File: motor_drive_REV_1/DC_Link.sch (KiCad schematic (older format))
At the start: 5 parts

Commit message: organizing pinout and BOM
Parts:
- removed M? (x2): Conn_01x01, symbol Connector_Generic:Conn_01x01
- removed R? (x2): R_Shunt, symbol motor_drive:R_Shunt
- added C13: 0.01uF, motor_drive_footprints:C_0603_1608Metric, symbol motor_drive:C
- added R19, R20: R, motor_drive_footprints:C_0603_1608Metric, symbol motor_drive:R
- R18: renamed from R?; footprint (none) -> motor_drive_footprints:C_0603_1608Metric
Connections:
- net labels added: 5.0V, DC_neg_in, DC_pos_in, GND
- net labels removed: DC+, DC-
- wire segments 12 -> 14
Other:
- moved on the sheet: R18
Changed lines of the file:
@@
 $Descr A4 11693 8268
 encoding utf-8
-Sheet 12 14
+Sheet 9 14
 Title ""
 Date ""
@@
 $EndDescr
 $Comp
-L Connector_Generic:Conn_01x01 M?
-U 1 1 5E3365D3
-P 4900 4150
-AR Path="/5E3365D3" Ref="M?"  Part="1"
-AR Path="/5E257703/5E3365D3" Ref="M?"  Part="1"
-F 0 "M?" H 4980 4146 50  0000 L CNN
-F 1 "Conn_01x01" H 4980 4101 50  0001 L CNN
-F 2 "" H 4900 4150 50  0001 C CNN
-F 3 "~" H 4900 4150 50  0001 C CNN
-	1    4900 4150
-	-1   0    0    1
-$EndComp
-$Comp
-L Connector_Generic:Conn_01x01 M?
-U 1 1 5E3365D9
-P 4900 2900
-AR Path="/5E3365D9" Ref="M?"  Part="1"
-AR Path="/5E257703/5E3365D9" Ref="M?"  Part="1"
-F 0 "M?" H 4980 2896 50  0000 L CNN
-F 1 "Conn_01x01" H 4980 2851 50  0001 L CNN
-F 2 "" H 4900 2900 50  0001 C CNN
-F 3 "~" H 4900 2900 50  0001 C CNN
-	1    4900 2900
-	-1   0    0    1
-$EndComp
-Text GLabel 6500 2900 2    50   Input ~ 0
-DC+
-Text GLabel 6550 4150 2    50   Input ~ 0
-DC-
-Wire Wire Line
-	5900 2900 5700 2900
-$Comp
-L motor_drive:R_Shunt R?
-U 1 1 5E3365E2
-P 5500 2900
-F 0 "R?" V 5275 2900 50  0000 C CNN
-F 1 "R_Shunt" V 5366 2900 50  0000 C CNN
-F 2 "" V 5430 2900 50  0001 C CNN
-F 3 "~" H 5500 2900 50  0001 C CNN
-	1    5500 2900
-	0    -1   -1   0
-$EndComp
-$Comp
-L motor_drive:R_Shunt R?
-U 1 1 5E3365E8
-P 5100 3800
-F 0 "R?" V 4875 3800 50  0000 C CNN
-F 1 "R_Shunt" V 4966 3800 50  0000 C CNN
-F 2 "" V 5030 3800 50  0001 C CNN
-F 3 "~" H 5100 3800 50  0001 C CNN
-	1    5100 3800
+L motor_drive:R R?
+U 1 1 5E3365EF
+P 3950 2500
+AR Path="/5E26944C/5E3365EF" Ref="R?"  Part="1"
+AR Path="/5E3365EF" Ref="R?"  Part="1"
+AR Path="/5E334D58/5E3365EF" Ref="R18"  Part="1"
+F 0 "R18" V 3743 2500 50  0000 C CNN
+F 1 "R" V 3834 2500 50  0000 C CNN
+F 2 "motor_drive_footprints:C_0603_1608Metric" V 3880 2500 50  0001 C CNN
+F 3 "~" H 3950 2500 50  0001 C CNN
+	1    3950 2500
 	1    0    0    -1
 $EndComp
 Wire Wire Line
-	5300 2900 5100 2900
+	3950 2100 3950 2350
+Text HLabel 5100 1500 2    50   Input ~ 0
+IDC_sense_p
+Text HLabel 5100 1750 2    50   Input ~ 0
+IDC_sense_n
+Text HLabel 5100 2100 2    50   Input ~ 0
+DC_pos_in
+Text HLabel 5100 2850 2    50   Input ~ 0
+VDC_sense_p
+Text HLabel 5100 3150 2    50   Input ~ 0
+VDC_sense_n
+Text HLabel 5100 3450 2    50   Input ~ 0
+DC_neg_in
 $Comp
 L motor_drive:R R?
-U 1 1 5E3365EF
-P 5100 3300
-AR Path="/5E26944C/5E3365EF" Ref="R?"  Part="1"
-AR Path="/5E3365EF" Ref="R?"  Part="1"
-F 0 "R?" V 4893 3300 50  0000 C CNN
-F 1 "R" V 4984 3300 50  0000 C CNN
-F 2 "" V 5030 3300 50  0001 C CNN
-F 3 "~" H 5100 3300 50  0001 C CNN
-	1    5100 3300
+U 1 1 5E35CBE4
+P 3950 3000
+AR Path="/5E26944C/5E35CBE4" Ref="R?"  Part="1"
+AR Path="/5E35CBE4" Ref="R?"  Part="1"
+AR Path="/5E334D58/5E35CBE4" Ref="R19"  Part="1"
+F 0 "R19" V 3743 3000 50  0000 C CNN
+F 1 "R" V 3834 3000 50  0000 C CNN
+F 2 "motor_drive_footprints:C_0603_1608Metric" V 3880 3000 50  0001 C CNN
+F 3 "~" H 3950 3000 50  0001 C CNN
+	1    3950 3000
 	1    0    0    -1
 $EndComp
+$Comp
+L motor_drive:R R?
+U 1 1 5E35DBC4
+P 4700 2100
+AR Path="/5E26944C/5E35DBC4" Ref="R?"  Part="1"
+AR Path="/5E35DBC4" Ref="R?"  Part="1"
+AR Path="/5E334D58/5E35DBC4" Ref="R20"  Part="1"
+F 0 "R20" V 4493 2100 50  0000 C CNN
+F 1 "R" V 4584 2100 50  0000 C CNN
+F 2 "motor_drive_footprints:C_0603_1608Metric" V 4630 2100 50  0001 C CNN
+F 3 "~" H 4700 2100 50  0001 C CNN
+	1    4700 2100
+	0    -1   -1   0
+$EndComp
 Wire Wire Line
-	5100 2900 5100 3150
-Connection ~ 5100 2900
+	4850 2100 5100 2100
 Wire Wire Line
-	5100 3450 5100 3600
+	4550 1500 4550 2100
+Connection ~ 4550 2100
 Wire Wire Line
-	5100 4000 5100 4150
+	3950 2650 3950 2850
+Text HLabel 3750 2100 0    50   Input ~ 0
+DC_pos
 Wire Wire Line
-	5100 4150 5900 4150
-Connection ~ 5100 4150
-Text GLabel 6550 3700 2    50   Input ~ 0
-VDC_sense_p
-Text GLabel 6550 3900 2    50   Input ~ 0
-VDC_sense_n
+	3750 2100 3950 2100
+Text HLabel 3750 3450 0    50   Input ~ 0
+DC_neg
 Wire Wire Line
-	5250 3900 5450 3900
+	3750 3450 3950 3450
 Wire Wire Line
-	5250 3700 5450 3700
-Text GLabel 6500 2300 2    50   Input ~ 0
-IDC_sense_p
-Text GLabel 6500 2500 2    50   Input ~ 0
-IDC_sense_n
+	3950 3150 3950 3450
+$Comp
+L motor_drive:C C?
+U 1 1 5E3AE82D
+P 3550 4950
+AR Path="/5E38D632/5E3AE82D" Ref="C?"  Part="1"
+AR Path="/5E334D58/5E3AE82D" Ref="C13"  Part="1"
+F 0 "C13" H 3665 4996 50  0000 L CNN
+F 1 "0.01uF" H 3665 4905 50  0000 L CNN
+F 2 "motor_drive_footprints:C_0603_1608Metric" H 3588 4800 50  0001 C CNN
+F 3 "~" H 3550 4950 50  0001 C CNN
+	1    3550 4950
+	1    0    0    -1
+$EndComp
+Text Label 3550 4800 0    50   ~ 0
+5.0V
+Text Label 3550 5100 0    50   ~ 0
+GND
+Text Label 4000 3450 0    50   ~ 0
+DC_neg
+Text Label 4000 2100 0    50   ~ 0
+DC_pos
 Wire Wire Line
-	5650 2500 5600 2500
+	3950 2100 4550 2100
+Connection ~ 3950 2100
 Wire Wire Line
-	5600 2500 5600 2750
+	3950 3450 5100 3450
+Connection ~ 3950 3450
+Connection ~ 3950 2850
+Connection ~ 3950 3150
 Wire Wire Line
-	5650 2300 5400 2300
+	5100 1750 4850 1750
 Wire Wire Line
-	5400 2300 5400 2750
-Text HLabel 5650 2300 2    50   Input ~ 0
-IDC_sense_p
-Text HLabel 5650 2500 2    50   Input ~ 0
-IDC_sense_n
-Text HLabel 5900 2900 2    50   Input ~ 0
-DC_pos
-Text HLabel 5450 3700 2    50   Input ~ 0
-VDC_sense_p
-Text HLabel 5450 3900 2    50   Input ~ 0
-VDC_sense_n
-Text HLabel 5900 4150 2    50   Input ~ 0
-DC_neg
+	4850 1750 4850 2100
+Connection ~ 4850 2100
+Wire Wire Line
+	4550 1500 5100 1500
+Wire Wire Line
+	3950 3150 5100 3150
+Wire Wire Line
+	3950 2850 5100 2850
 $EndSCHEMATC

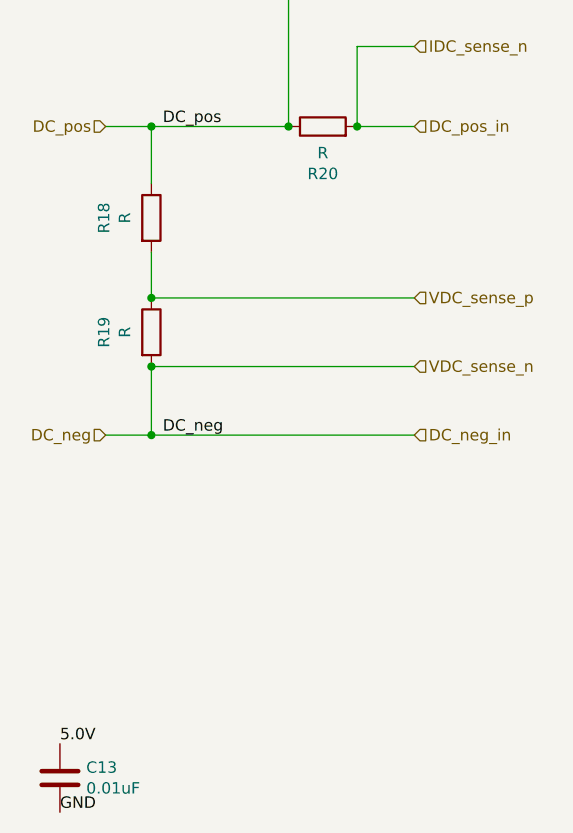
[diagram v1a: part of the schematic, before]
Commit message: working on adding thermistors but encountered too many hierarchicaly copies bug
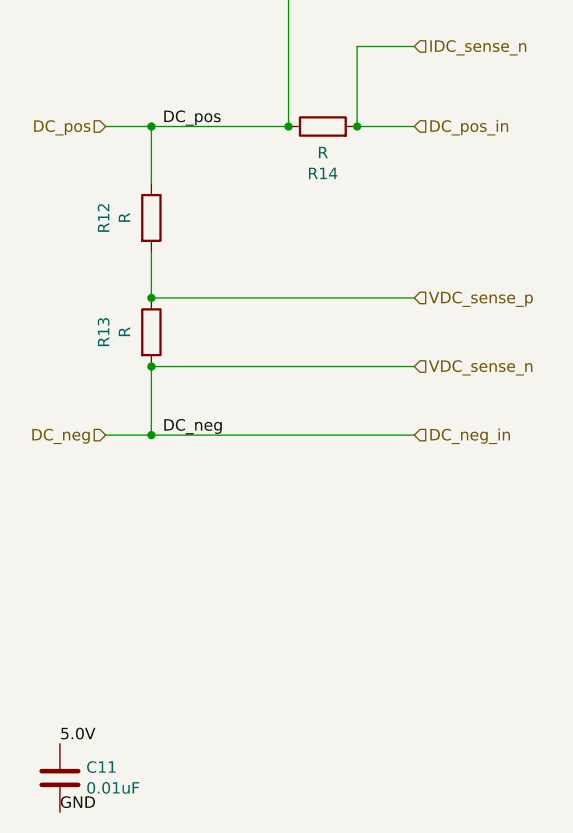
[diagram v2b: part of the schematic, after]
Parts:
- renumbered C13 to C11, R18 to R12, R19 to R13, R20 to R14
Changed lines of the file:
@@
 AR Path="/5E26944C/5E3365EF" Ref="R?"  Part="1"
 AR Path="/5E3365EF" Ref="R?"  Part="1"
-AR Path="/5E334D58/5E3365EF" Ref="R18"  Part="1"
-F 0 "R18" V 3743 2500 50  0000 C CNN
+AR Path="/5E334D58/5E3365EF" Ref="R12"  Part="1"
+F 0 "R12" V 3743 2500 50  0000 C CNN
 F 1 "R" V 3834 2500 50  0000 C CNN
 F 2 "motor_drive_footprints:C_0603_1608Metric" V 3880 2500 50  0001 C CNN
@@
 AR Path="/5E26944C/5E35CBE4" Ref="R?"  Part="1"
 AR Path="/5E35CBE4" Ref="R?"  Part="1"
-AR Path="/5E334D58/5E35CBE4" Ref="R19"  Part="1"
-F 0 "R19" V 3743 3000 50  0000 C CNN
+AR Path="/5E334D58/5E35CBE4" Ref="R13"  Part="1"
+F 0 "R13" V 3743 3000 50  0000 C CNN
 F 1 "R" V 3834 3000 50  0000 C CNN
 F 2 "motor_drive_footprints:C_0603_1608Metric" V 3880 3000 50  0001 C CNN
@@
 AR Path="/5E26944C/5E35DBC4" Ref="R?"  Part="1"
 AR Path="/5E35DBC4" Ref="R?"  Part="1"
-AR Path="/5E334D58/5E35DBC4" Ref="R20"  Part="1"
-F 0 "R20" V 4493 2100 50  0000 C CNN
+AR Path="/5E334D58/5E35DBC4" Ref="R14"  Part="1"
+F 0 "R14" V 4493 2100 50  0000 C CNN
 F 1 "R" V 4584 2100 50  0000 C CNN
 F 2 "motor_drive_footprints:C_0603_1608Metric" V 4630 2100 50  0001 C CNN
@@
 P 3550 4950
 AR Path="/5E38D632/5E3AE82D" Ref="C?"  Part="1"
-AR Path="/5E334D58/5E3AE82D" Ref="C13"  Part="1"
-F 0 "C13" H 3665 4996 50  0000 L CNN
+AR Path="/5E334D58/5E3AE82D" Ref="C11"  Part="1"
+F 0 "C11" H 3665 4996 50  0000 L CNN
 F 1 "0.01uF" H 3665 4905 50  0000 L CNN
 F 2 "motor_drive_footprints:C_0603_1608Metric" H 3588 4800 50  0001 C CNN

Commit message: started layout
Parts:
- added C10, C12, C13, C14, C15, C16, C17, C18, C19, C20, C9: 1uF, motor_drive_footprints:gen_0805, symbol motor_drive:C
- C11: value 0.01uF -> 1uF; footprint motor_drive_footprints:C_0603_1608Metric -> motor_drive_footprints:gen_0805
- renumbered R14 to R10, R12 to R11, R13 to R12
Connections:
- net 5.0V: now also C10.1, C13.1, C14.1, C15.1, C16.1, C17.1, C18.1, C19.1, C20.1, C9.1; no longer C11.1
- net DC_neg: now also C12.2
- net DC_pos: now also C11.1
- net GND: now also C10.2, C13.2, C14.2, C15.2, C16.2, C17.2, C18.2, C19.2, C20.2, C9.2; no longer C11.2
- new net phase_shield: C11.2, C12.1
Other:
- moved on the sheet: R10, R11, R12

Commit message: gate drive rework and schematic re-organization
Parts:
- renumbered R10 to R7, R11 to R8, R12 to R9
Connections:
- net 5.0V is gone; now on net DC_pos: C10.1, C13.1, C14.1, C15.1, C16.1, C17.1, C18.1, C19.1, C20.1, C9.1
- net GND is gone; now on net DC_neg: C10.2, C13.2, C14.2, C15.2, C16.2, C17.2, C18.2, C19.2, C20.2, C9.2
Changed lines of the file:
@@
 $Descr A4 11693 8268
 encoding utf-8
-Sheet 9 16
+Sheet 6 8
 Title ""
 Date ""
@@
 AR Path="/5E26944C/5E3365EF" Ref="R?"  Part="1"
 AR Path="/5E3365EF" Ref="R?"  Part="1"
-AR Path="/5E334D58/5E3365EF" Ref="R11"  Part="1"
-F 0 "R11" V 3943 3000 50  0000 C CNN
+AR Path="/5E334D58/5E3365EF" Ref="R8"  Part="1"
+F 0 "R8" V 3943 3000 50  0000 C CNN
 F 1 "R" V 4034 3000 50  0000 C CNN
 F 2 "motor_drive_footprints:C_0603_1608Metric" V 4080 3000 50  0001 C CNN
@@
 Text HLabel 4350 3300 2    50   Input ~ 0
 VDC_sense_p
-Text HLabel 4350 3700 2    50   Input ~ 0
-VDC_sense_n
-Text HLabel 2600 3950 0    50   Input ~ 0
-DC_neg_in
 $Comp
 L motor_drive:R R?
@@
 AR Path="/5E26944C/5E35CBE4" Ref="R?"  Part="1"
 AR Path="/5E35CBE4" Ref="R?"  Part="1"
-AR Path="/5E334D58/5E35CBE4" Ref="R12"  Part="1"
-F 0 "R12" V 3943 3500 50  0000 C CNN
+AR Path="/5E334D58/5E35CBE4" Ref="R9"  Part="1"
+F 0 "R9" V 3943 3500 50  0000 C CNN
 F 1 "R" V 4034 3500 50  0000 C CNN
 F 2 "motor_drive_footprints:C_0603_1608Metric" V 4080 3500 50  0001 C CNN
@@
 AR Path="/5E26944C/5E35DBC4" Ref="R?"  Part="1"
 AR Path="/5E35DBC4" Ref="R?"  Part="1"
-AR Path="/5E334D58/5E35DBC4" Ref="R10"  Part="1"
-F 0 "R10" V 3193 2650 50  0000 C CNN
+AR Path="/5E334D58/5E35DBC4" Ref="R7"  Part="1"
+F 0 "R7" V 3193 2650 50  0000 C CNN
 F 1 "R" V 3284 2650 50  0000 C CNN
 F 2 "motor_drive_footprints:C_0603_1608Metric" V 3330 2650 50  0001 C CNN
@@
 Text HLabel 4350 3950 2    50   Input ~ 0
 DC_neg
-Wire Wire Line
-	4150 3650 4150 3700
-Text Label 3850 3950 0    50   ~ 0
+Text Label 4150 3950 0    50   ~ 0
 DC_neg
 Text Label 4100 2650 2    50   ~ 0
@@
 $EndComp
 Text Label 6800 2650 0    50   ~ 0
-5.0V
+DC_pos
 Text Label 6800 2950 0    50   ~ 0
-GND
+DC_neg
 $Comp
 L motor_drive:C C?
@@
 $EndComp
 Text Label 6800 3650 0    50   ~ 0
-5.0V
+DC_pos
 Text Label 6800 3950 0    50   ~ 0
-GND
+DC_neg
 $Comp
 L motor_drive:C C?
@@
 	2600 3250 3550 3250
 Wire Wire Line
-	2600 3950 4150 3950
-Wire Wire Line
 	4350 3300 4150 3300
 Connection ~ 4150 3300
@@
 	4150 3300 4150 3350
 Wire Wire Line
-	4150 3700 4350 3700
-Connection ~ 4150 3700
-Wire Wire Line
-	4150 3700 4150 3950
-Wire Wire Line
 	4150 3950 4350 3950
-Connection ~ 4150 3950
 $Comp
 L motor_drive:C C?
@@
 Wire Wire Line
 	6600 5300 6600 5400
+Wire Wire Line
+	4150 3650 4150 3950
 $EndSCHEMATC
